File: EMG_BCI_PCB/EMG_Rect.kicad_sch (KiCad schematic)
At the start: 24 parts, among them J2 2.54 mm header, U3 ADA4807-4ARUZ, U8 MCP1501-18xCH

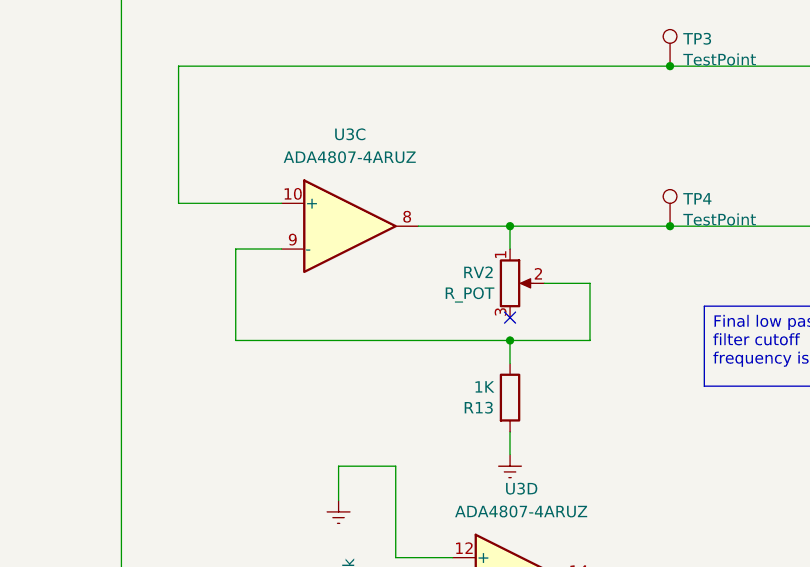
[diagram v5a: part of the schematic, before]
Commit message: Ran ERC again
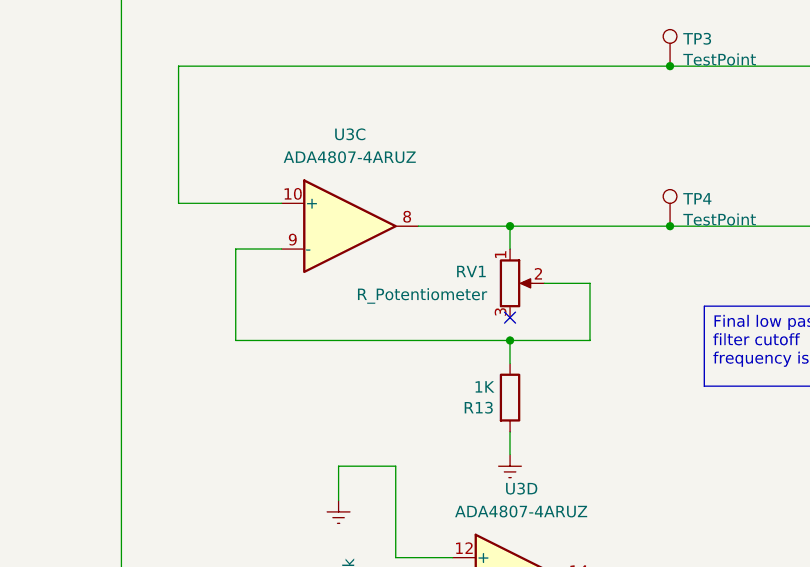
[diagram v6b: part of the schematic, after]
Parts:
- removed RV2: R_POT, Potentiometer_THT:Potentiometer_Piher_PT-10-V10_Vertical, symbol Device:R_POT
- added RV1: R_Potentiometer, symbol Device:R_Potentiometer
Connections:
- net at R17.2, TP4.1, U3.8: now also RV1.1
- net at R13.1, U3.9 (-): now also RV1.2
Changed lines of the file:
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@@
-	)
-	(symbol
-		(lib_id "Device:R_POT")
-		(at 113.03 93.98 0)
-		(unit 1)
-		(exclude_from_sim no)
-		(in_bom yes)
-		(on_board yes)
-		(dnp no)
-		(property "Reference" "RV2"
-			(at 111.2774 92.8116 0)
-			(effects
-				(font
-					(size 1.27 1.27)
-				)
-				(justify right)
-			)
-		)
-		(property "Value" "R_POT"
-			(at 111.2774 95.123 0)
-			(effects
-				(font
-					(size 1.27 1.27)
-				)
-				(justify right)
-			)
-		)
-		(property "Footprint" "Potentiometer_THT:Potentiometer_Piher_PT-10-V10_Vertical"
-			(at 113.03 93.98 0)
-			(effects
-				(font
-					(size 1.27 1.27)
-				)
-				(hide yes)
-			)
-		)
-		(property "Datasheet" "~"
-			(at 113.03 93.98 0)
-			(effects
-				(font
-					(size 1.27 1.27)
-				)
-				(hide yes)
-			)
-		)
-		(property "Description" ""
-			(at 113.03 93.98 0)
-			(effects
-				(font
-					(size 1.27 1.27)
-				)
-			)
-		)
-		(pin "3"
-		)
-		(pin "1"
-		)
-		(pin "2"
-		)
-		(instances
-			(project "EMG_BCI_PCB"
-				(path "/55cf2478-b5ba-45ce-afa6-3f75a1bb5fb4/00000000-0000-0000-0000-00005f16ee03"
-					(reference "RV2")
-					(unit 1)
-				)
-			)
-		)
 	)
 	(symbol
@@
 					(unit 1)
 				)
+			)
+		)
+	)
+	(symbol
+		(lib_id "Device:R_Potentiometer")
+		(at 113.03 93.98 0)
+		(unit 1)
+		(exclude_from_sim no)
+		(in_bom yes)
+		(on_board yes)
+		(dnp no)
+		(fields_autoplaced yes)
+		(property "Reference" "RV1"
+			(at 110.49 92.7099 0)
+			(effects
+				(font
+					(size 1.27 1.27)
+				)
+				(justify right)
+			)
+		)
+		(property "Value" "R_Potentiometer"
+			(at 110.49 95.2499 0)
+			(effects
+				(font
+					(size 1.27 1.27)
+				)
+				(justify right)
+			)
+		)
+		(property "Footprint" ""
+			(at 113.03 93.98 0)
+			(effects
+				(font
+					(size 1.27 1.27)
+				)
+				(hide yes)
+			)
+		)
+		(property "Datasheet" "~"
+			(at 113.03 93.98 0)
+			(effects
+				(font
+					(size 1.27 1.27)
+				)
+				(hide yes)
+			)
+		)
+		(property "Description" "Potentiometer"
+			(at 113.03 93.98 0)
+			(effects
+				(font
+					(size 1.27 1.27)
+				)
+				(hide yes)
+			)
+		)
+		(pin "3"
+		)
+		(pin "1"
+		)
+		(pin "2"
+		)
+		(instances
+			(project ""
+				(path "/55cf2478-b5ba-45ce-afa6-3f75a1bb5fb4/00000000-0000-0000-0000-00005f16ee03"
+					(reference "RV1")
+					(unit 1)
+				)

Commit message: Imported footprints into layout
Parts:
- RV1: footprint (none) -> Potentiometer_THT:Potentiometer_Piher_PT-10-V10_Vertical
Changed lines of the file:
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@@
 			)
 		)
-		(property "Footprint" ""
+		(property "Footprint" "Potentiometer_THT:Potentiometer_Piher_PT-10-V10_Vertical"
 			(at 113.03 93.98 0)
 			(effects

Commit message: Initial placement and routing
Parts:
- C17, C18, C19, C20, C21, C22, C5, C7: footprint Capacitor_SMD:C_0201_0603Metric_Pad0.64x0.40mm_HandSolder -> Capacitor_SMD:C_0603_1608Metric_Pad1.08x0.95mm_HandSolder
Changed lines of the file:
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@@
 			)
 		)
-		(property "Footprint" "Capacitor_SMD:C_0201_0603Metric_Pad0.64x0.40mm_HandSolder"
+		(property "Footprint" "Capacitor_SMD:C_0603_1608Metric_Pad1.08x0.95mm_HandSolder"
 			(at 169.8752 99.06 0)
 			(effects
@@
 			)
 		)
-		(property "Footprint" "Capacitor_SMD:C_0201_0603Metric_Pad0.64x0.40mm_HandSolder"
+		(property "Footprint" "Capacitor_SMD:C_0603_1608Metric_Pad1.08x0.95mm_HandSolder"
 			(at 117.8052 48.26 0)
 			(effects
@@
 			)
 		)
-		(property "Footprint" "Capacitor_SMD:C_0201_0603Metric_Pad0.64x0.40mm_HandSolder"
+		(property "Footprint" "Capacitor_SMD:C_0603_1608Metric_Pad1.08x0.95mm_HandSolder"
 			(at 223.2152 67.31 0)
 			(effects
@@
 			)
 		)
-		(property "Footprint" "Capacitor_SMD:C_0201_0603Metric_Pad0.64x0.40mm_HandSolder"
+		(property "Footprint" "Capacitor_SMD:C_0603_1608Metric_Pad1.08x0.95mm_HandSolder"
 			(at 234.6452 67.31 0)
 			(effects
@@
 			)
 		)
-		(property "Footprint" "Capacitor_SMD:C_0201_0603Metric_Pad0.64x0.40mm_HandSolder"
+		(property "Footprint" "Capacitor_SMD:C_0603_1608Metric_Pad1.08x0.95mm_HandSolder"
 			(at 223.2152 38.1 0)
 			(effects
@@
 			)
 		)
-		(property "Footprint" "Capacitor_SMD:C_0201_0603Metric_Pad0.64x0.40mm_HandSolder"
+		(property "Footprint" "Capacitor_SMD:C_0603_1608Metric_Pad1.08x0.95mm_HandSolder"
 			(at 234.6452 38.1 0)
 			(effects
@@
 			)
 		)
-		(property "Footprint" "Capacitor_SMD:C_0201_0603Metric_Pad0.64x0.40mm_HandSolder"
+		(property "Footprint" "Capacitor_SMD:C_0603_1608Metric_Pad1.08x0.95mm_HandSolder"
 			(at 63.8048 146.05 0)
 			(effects
@@
 			)
 		)
-		(property "Footprint" "Capacitor_SMD:C_0201_0603Metric_Pad0.64x0.40mm_HandSolder"
+		(property "Footprint" "Capacitor_SMD:C_0603_1608Metric_Pad1.08x0.95mm_HandSolder"
 			(at 24.4348 146.05 0)
 			(effects
